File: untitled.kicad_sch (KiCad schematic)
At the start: 13 parts, among them J2 J_000001, J3 J_000001, U2 PWR_nPM1100-QDXX

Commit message: added schmatic symbols and footprints for key capacitors, selected LCXO crystal to use internal caps
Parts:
- R15, R3, R5: footprint (none) -> Resistor_SMD:R_0402_1005Metric; LCSC PNs (none) -> C25744; MPNs (none) -> 0402WGF1002TCE
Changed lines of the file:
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@@
 			)
 		)
-		(property "Footprint" ""
+		(property "Footprint" "Resistor_SMD:R_0402_1005Metric"
 			(at 165.1 93.98 0)
 			(effects
@@
 			)
 		)
-		(property "Description" "10kΩ resistor"
+		(property "Description" "10kΩ resistor 0402"
 			(at 165.1 93.98 0)
 			(effects
@@
 			)
 		)
-		(property "MPNs" ""
+		(property "MPNs" "0402WGF1002TCE"
 			(at 165.1 93.98 0)
 			(effects
@@
 			)
 		)
-		(property "LCSC PNs" ""
+		(property "LCSC PNs" "C25744"
 			(at 165.1 93.98 0)
 			(effects
@@
 			)
 		)
-		(property "Footprint" ""
+		(property "Footprint" "Resistor_SMD:R_0402_1005Metric"
 			(at 92.71 80.01 0)
 			(effects
@@
 			)
 		)
-		(property "Description" "10kΩ resistor"
+		(property "Description" "10kΩ resistor 0402"
 			(at 92.71 80.01 0)
 			(effects
@@
 			)
 		)
-		(property "MPNs" ""
+		(property "MPNs" "0402WGF1002TCE"
 			(at 92.71 80.01 0)
 			(effects
@@
 			)
 		)
-		(property "LCSC PNs" ""
+		(property "LCSC PNs" "C25744"
 			(at 92.71 80.01 0)
 			(effects
@@
 			)
 		)
-		(property "Footprint" ""
+		(property "Footprint" "Resistor_SMD:R_0402_1005Metric"
 			(at 93.98 114.3 0)
 			(effects
@@
 			)
 		)
-		(property "Description" "10kΩ resistor"
+		(property "Description" "10kΩ resistor 0402"
 			(at 93.98 114.3 0)
 			(effects
@@
 			)
 		)
-		(property "MPNs" ""
+		(property "MPNs" "0402WGF1002TCE"
 			(at 93.98 114.3 0)
 			(effects
@@
 			)
 		)
-		(property "LCSC PNs" ""
+		(property "LCSC PNs" "C25744"
 			(at 93.98 114.3 0)
 			(effects

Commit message: added SMD indicator LED symbol & footprint
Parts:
- J2: footprint (none) -> Connector_USB:USB_C_Receptacle_GCT_USB4135-GF-A_6P_TopMnt_Horizontal
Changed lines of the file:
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@@
 			)
 		)
-		(property "Footprint" ""
+		(property "Footprint" "Connector_USB:USB_C_Receptacle_GCT_USB4135-GF-A_6P_TopMnt_Horizontal"
 			(at 171.704 47.498 0)
 			(effects

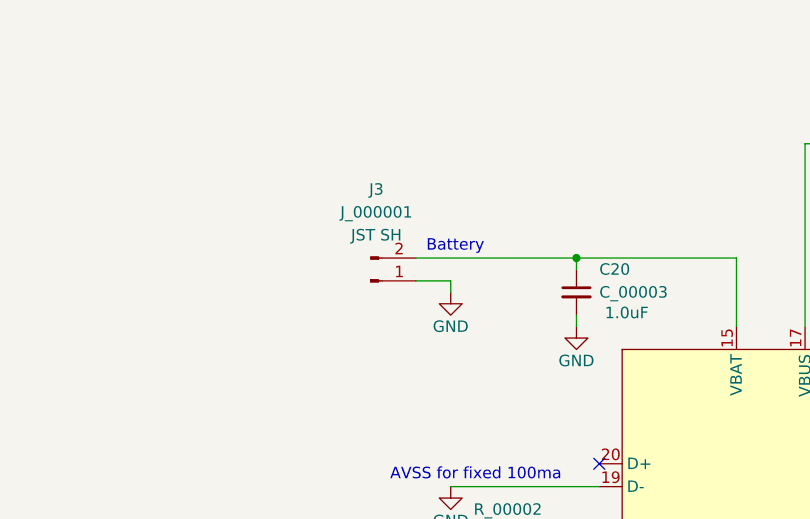
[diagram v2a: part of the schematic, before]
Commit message: added JST connector symbol + footprint
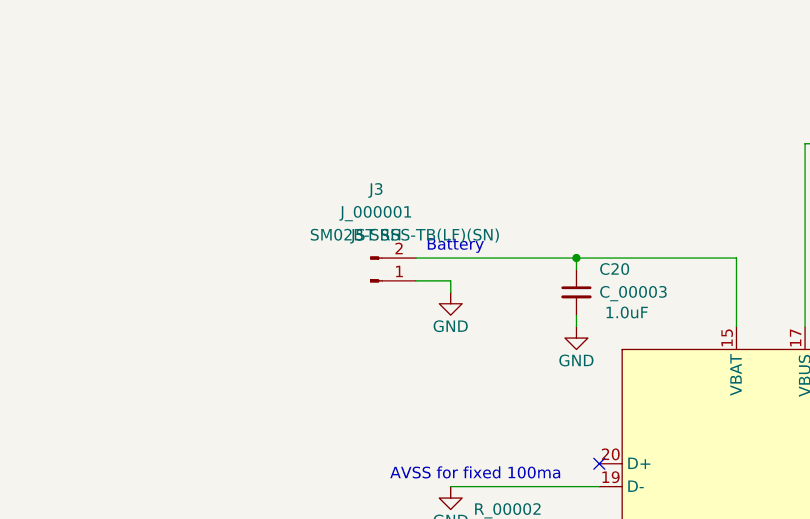
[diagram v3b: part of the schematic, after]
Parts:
- J3: footprint (none) -> mic_patch_parts:J_000001; LCSC PNs (none) -> C160402; MPNs (none) -> SM02B-SRSS-TB(LF)(SN)
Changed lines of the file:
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@@
 	)
 	(symbol
+		(lib_name "J_000001_1")
 		(lib_id "mic_patch_parts:J_000001")
 		(at 81.28 44.45 180)
@@
 			)
 		)
-		(property "Footprint" ""
+		(property "Footprint" "mic_patch_parts:J_000001"
 			(at 74.676 36.322 0)
 			(effects
@@
 			)
 		)
-		(property "Description" "JST SH Pin Connector"
+		(property "Description" "JST SH 2 Right Angled Pin Connector"
 			(at 78.486 55.626 0)
 			(effects
@@
 			)
 		)
-		(property "LCSC PNs" ""
+		(property "LCSC PNs" "C160402"
 			(at 79.756 42.672 0)
 			(effects
@@
 			)
 		)
+		(property "MPNs" "SM02B-SRSS-TB(LF)(SN) "
+			(at 81.28 44.45 0)
+			(effects
+				(font
+					(size 1.27 1.27)
+				)
+			)
+		)

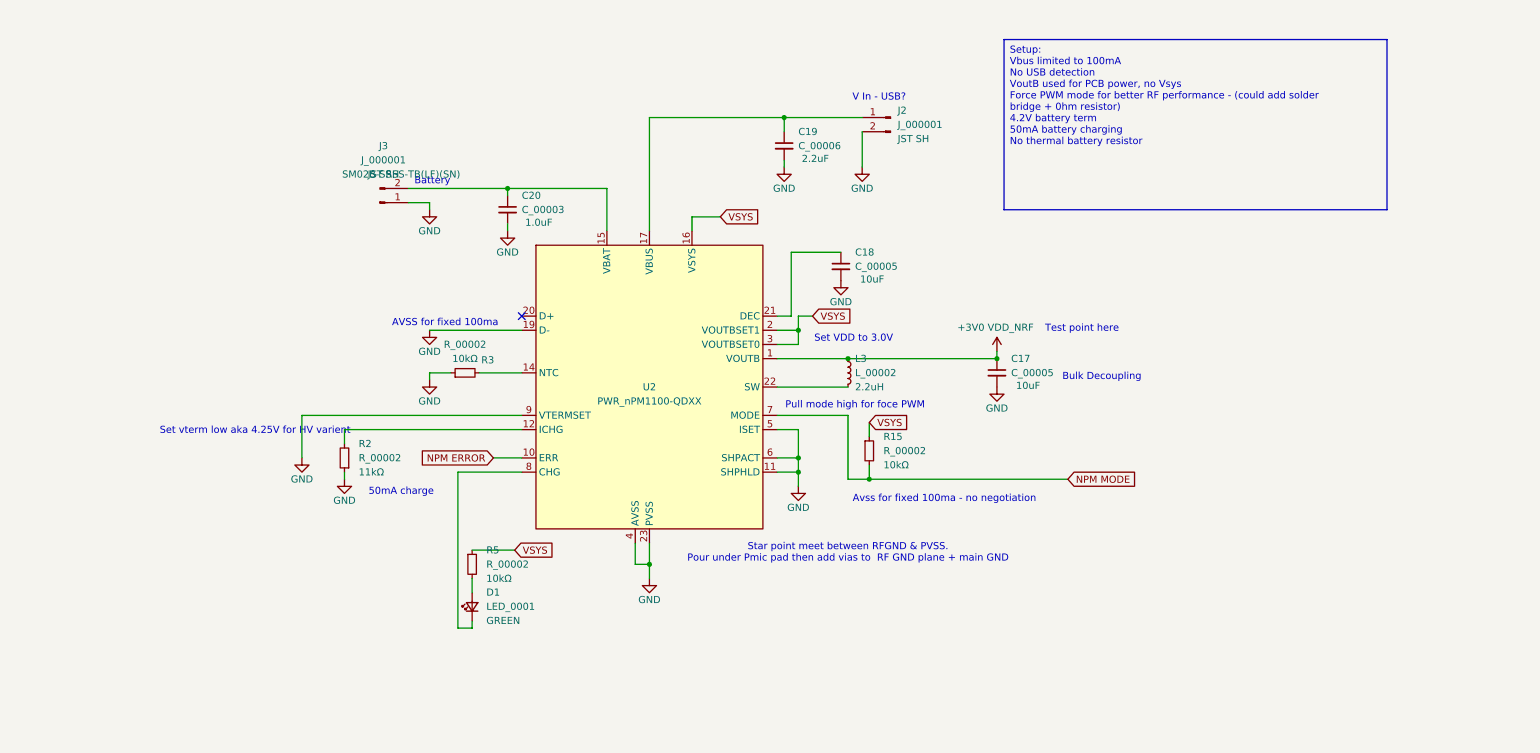
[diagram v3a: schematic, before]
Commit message: added all footprints for power module
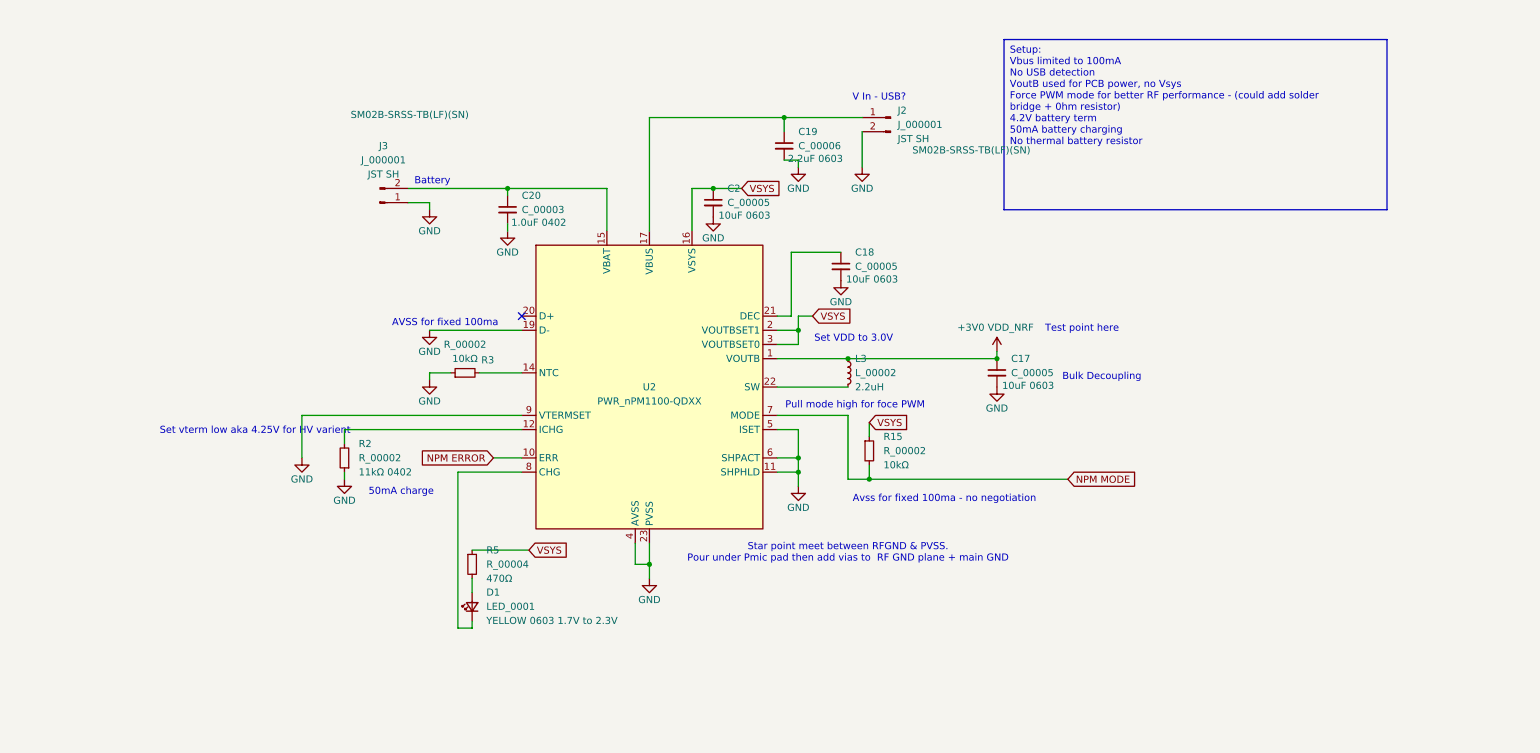
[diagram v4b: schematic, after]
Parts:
- removed R5: R_00002, Resistor_SMD:R_0402_1005Metric, symbol mic_patch_parts:R_00003
- added C2: C_00005, Capacitor_SMD:C_0603_1608Metric, symbol mic_patch_parts:C_00005
- added R5: R_00004, Resistor_SMD:R_0402_1005Metric, symbol mic_patch_parts:R_00004
- C17, C18: footprint (none) -> Capacitor_SMD:C_0603_1608Metric; LCSC PNs (none) -> C19702; MPNs (none) -> CL10A106KP8NNNC
- C19: LCSC PNs (none) -> C23630; MPNs (none) -> CL10A225KO8NNNC
- C20: footprint (none) -> Capacitor_SMD:C_0402_1005Metric; LCSC PNs (none) -> C52923; MPNs (none) -> CL05A105KA5NQNC
- D1: footprint (none) -> LED_SMD:LED_0603_1608Metric; Desc GREEN -> YELLOW 0603 1.7V to 2.3V; LCSC PNs (none) -> C72038; MPNs (none) -> 19-213/Y2C-CQ2R2L/3T(CY)
- J2: footprint Connector_USB:USB_C_Receptacle_GCT_USB4135-GF-A_6P_TopMnt_Horizontal -> mic_patch_parts:J_000001; LCSC PNs (none) -> C160402; MPNs (none) -> SM02B-SRSS-TB(LF)(SN)
- L3: footprint (none) -> Inductor_SMD:L_0805_2012Metric; LCSC PNs (none) -> C1043; MFNs (none) -> CMI201209U2R2KT
- R2: footprint (none) -> Resistor_SMD:R_0402_1005Metric; Desc 11kΩ -> 11kΩ 0402; LCSC PNs (none) -> C25749; MPNs (none) -> 0402WGF1102TCE
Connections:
- net GND: now also C2.2
- net VSYS: now also C2.1, R5.1
- net at D1.2 (A): now also R5.2

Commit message: Added USB symbol + 5.1k pull downs
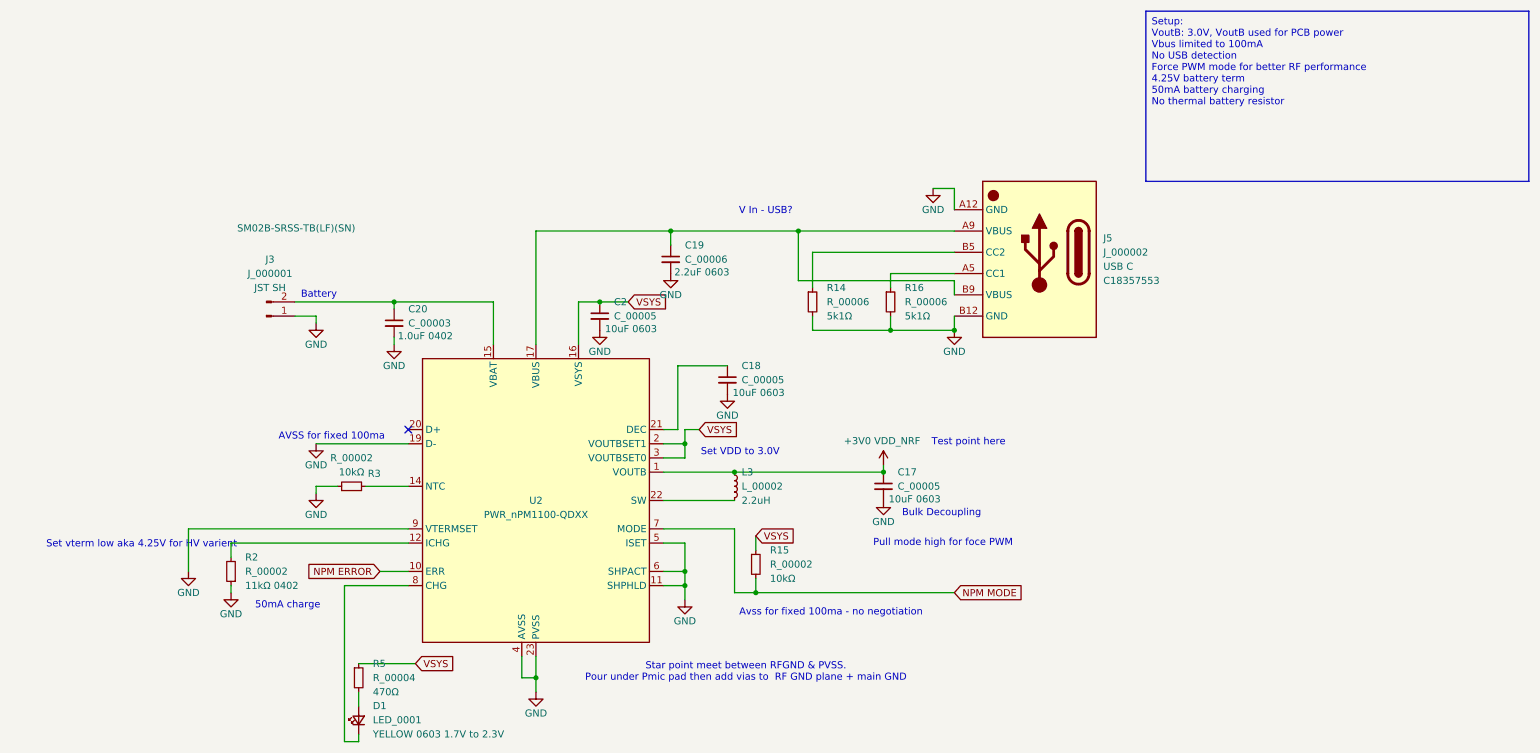
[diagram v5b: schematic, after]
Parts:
- removed J2: J_000001, mic_patch_parts:J_000001, symbol mic_patch_parts:J_000001
- added J5: J_000002, symbol mic_patch_parts:1000009
- added R14, R16: R_00006, Resistor_SMD:R_0402_1005Metric, symbol mic_patch_parts:R_00006
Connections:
- net GND: now also J5.A12 (GND), J5.B12 (GND), R14.2, R16.2
- net at C19.1, U2.17 (VBUS): now also J5.A9 (VBUS), J5.B9 (VBUS)
- new net: J5.A5 (CC1), R16.1
- new net: J5.B5 (CC2), R14.1
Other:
- moved on the sheet: C17, C18, C19, C2, C20, D1, J3, L3, R15, R2, R3, R5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

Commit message: added footprints for every part
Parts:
- C19: footprint (none) -> Capacitor_SMD:C_0201_0603Metric
- J5: footprint (none) -> mic_patch_parts:C5260493
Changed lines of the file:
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@@
 			)
 		)
-		(property "Footprint" ""
+		(property "Footprint" "mic_patch_parts:C5260493"
 			(at 194.564 78.232 0)
 			(effects
@@
 			)
 		)
-		(property "Footprint" ""
+		(property "Footprint" "Capacitor_SMD:C_0201_0603Metric"
 			(at 104.14 60.96 0)
 			(effects
